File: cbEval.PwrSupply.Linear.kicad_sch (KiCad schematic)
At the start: 34 parts, among them J1 CAL.CT3151V1-0, J11 Bergstik-II_6, J12 Header.Hor.2x8.9-103326-0-08, J13 Header.Hor.2x8.9-103326-0-08, J2 CAL.CT3151V1-2, J3 Socket.Hor.2x8.1-5535512-8, J4 Socket.Hor.2x8.1-5535512-8, U1 MIC29151-5.0WU, U2 MIC29151-3.3WU, U3 DS1834AS+

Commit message: Properties geändert, Logo aktualisiert
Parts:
- removed MP1: KiCAD-Logo2.5mm.SilkScreen, Symbol:KiCad-Logo2_5mm_SilkScreen, symbol Symbol:KiCAD-Logo2.5mm.SilkScreen
- added MP1: KiCAD-DesignedWith-Logo2.5mm.SilkScreen, Symbol:KiCad-Logo2_5mm_SilkScreen, symbol Symbol:KiCAD-DesignedWith-Logo2.5mm.SilkScreen
- J12, J3: Usage Usage -> Pwr Bus
- J13, J4: Usage Usage -> Data Bus
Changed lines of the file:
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@@
-    )
-  )
-  (symbol (lib_id "Symbol:KiCAD-Logo2.5mm.SilkScreen") (at 55.88 15.24 0) (unit 1)
-    (in_bom yes) (on_board yes)
-    (property "Reference" "MP1" (id 0) (at 55.88 15.24 0))
-    (property "Value" "KiCAD-Logo2.5mm.SilkScreen" (id 1) (at 55.88 17.78 0))
-    (property "Footprint" "Symbol:KiCad-Logo2_5mm_SilkScreen" (id 2) (at 55.88 12.7 0)
-      (effects (font (size 1.27 1.27)) hide)
-    )
-    (property "Datasheet" "" (id 3) (at 55.88 15.24 0)
-      (effects (font (size 1.27 1.27)) hide)
     )
   )
@@
     )
     (pin "1")
+  )
+  (symbol (lib_id "Symbol:KiCAD-DesignedWith-Logo2.5mm.SilkScreen") (at 55.88 15.24 0) (unit 1)
+    (in_bom yes) (on_board yes)
+    (property "Reference" "MP1" (id 0) (at 55.88 15.24 0))
+    (property "Value" "KiCAD-DesignedWith-Logo2.5mm.SilkScreen" (id 1) (at 55.88 17.78 0))
+    (property "Footprint" "Symbol:KiCad-Logo2_5mm_SilkScreen" (id 2) (at 55.88 12.7 0)
+      (effects (font (size 1.27 1.27)) hide)
+    )
+    (property "Datasheet" "" (id 3) (at 55.88 15.24 0)
+      (effects (font (size 1.27 1.27)) hide)
+    )
   )
   (symbol (lib_id "Supply:GND") (at 33.02 193.04 0) (unit 1)
@@
     (pin "2")
   )
-  (symbol (lib_name "C.Nichicon.UWT.35V:100µ_1") (lib_id "C.Nichicon.UWT.35V:100µ") (at 104.14 48.26 0) (mirror y) (unit 1)
+  (symbol (lib_id "C.Nichicon.UWT.35V:100µ") (at 104.14 48.26 0) (mirror y) (unit 1)
     (in_bom yes) (on_board yes)
     (property "Reference" "C1" (id 0) (at 101.6 43.18 0)
@@
       (effects (font (size 1.016 1.016)) hide)
     )
-    (property "Usage" "Usage" (id 4) (at 76.2 193.04 0))
+    (property "Usage" "Pwr Bus" (id 4) (at 76.2 193.04 0))
     (property "ID" "1-5535512-8" (id 5) (at 80.01 171.45 90)
       (effects (font (size 0.635 0.635) italic))
@@
       (effects (font (size 1.016 1.016)) hide)
     )
-    (property "Usage" "Usage" (id 4) (at 152.4 193.04 0))
+    (property "Usage" "Data Bus" (id 4) (at 152.4 193.04 0))
     (property "ID" "1-5535512-8" (id 5) (at 156.21 171.45 90)
       (effects (font (size 0.635 0.635) italic))
@@
       (effects (font (size 1.016 1.016)) hide)
     )
-    (property "Usage" "Usage" (id 4) (at 25.4 193.04 0))
+    (property "Usage" "Pwr Bus" (id 4) (at 25.4 193.04 0))
     (property "ID" "9-103326-0-08" (id 5) (at 21.59 171.45 90)
       (effects (font (size 0.635 0.635) italic))
@@
       (effects (font (size 1.016 1.016)) hide)
     )
-    (property "Usage" "Usage" (id 4) (at 109.22 193.04 0))
+    (property "Usage" "Data Bus" (id 4) (at 109.22 193.04 0))
     (property "ID" "9-103326-0-08" (id 5) (at 105.41 171.45 90)
       (effects (font (size 0.635 0.635) italic))
@@
       (reference "J13") (unit 1) (value "Header.Hor.2x8.9-103326-0-08") (footprint "Connector_PinHeader_2.54mm:PinHeader_2x08_P2.54mm_Horizontal")
     )
-    (path "/aa3513d0-0eee-457c-a792-7c9954431f2c"
-      (reference "MP1") (unit 1) (value "KiCAD-Logo2.5mm.SilkScreen") (footprint "Symbol:KiCad-Logo2_5mm_SilkScreen")
+    (path "/c9e57e62-be33-4183-8d54-8f35a9c1b2d9"
+      (reference "MP1") (unit 1) (value "KiCAD-DesignedWith-Logo2.5mm.SilkScreen") (footprint "Symbol:KiCad-Logo2_5mm_SilkScreen")
     )
     (path "/92587325-892b-4776-9d98-5bf9e0f65dcf"

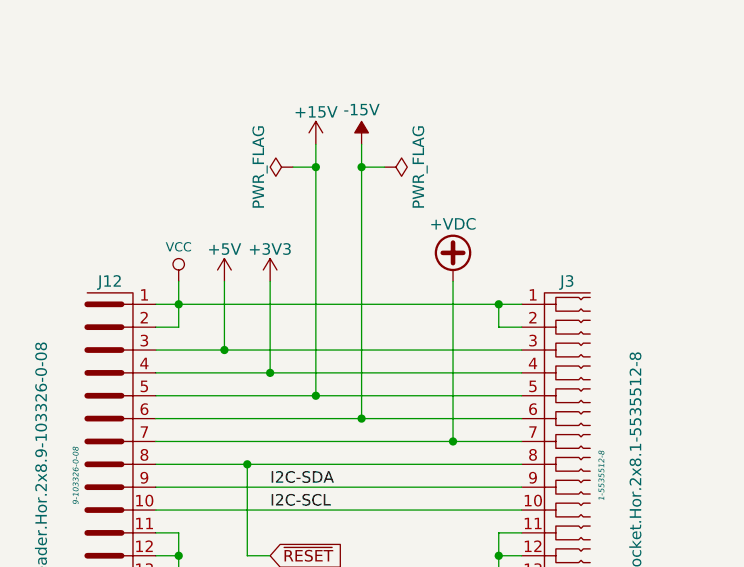
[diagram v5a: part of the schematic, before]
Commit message: Stromversorgung korrigiert (5P/3P3)
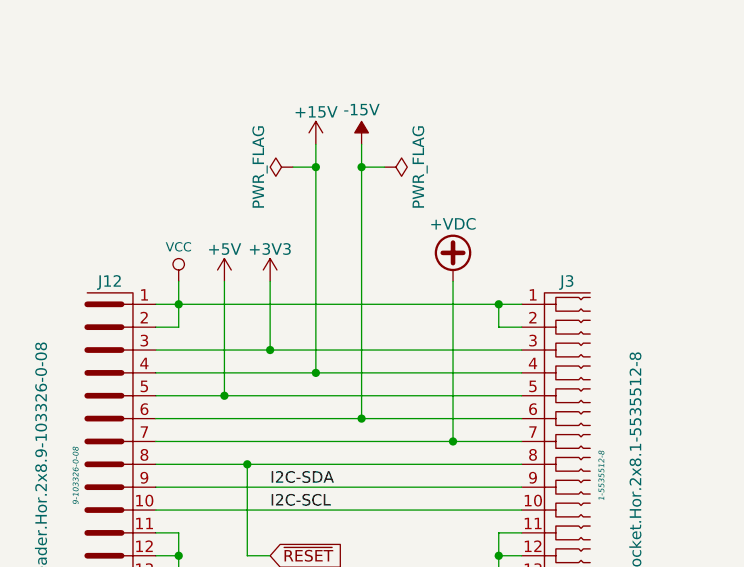
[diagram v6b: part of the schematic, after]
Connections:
- net +15V: now also J12.4, J3.4; no longer J12.5, J3.5
- net +3V3: now also J12.3, J3.3; no longer J12.4, J3.4
- net +5V: now also J12.5, J3.5; no longer J12.3, J3.3
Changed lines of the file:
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@@
-(kicad_sch (version 20210126) (generator eeschema)
+(kicad_sch (version 20210406) (generator eeschema)
   (paper "A4")
   (title_block
     (title "cbEval PSupply 5P/3P3")
-    (rev "1.0.0")
+    (rev "1.1.0")
   )
   (junction (at 33.02 152.4) (diameter 0.9144) (color 0 0 0 0))
@@
   (junction (at 35.56 73.66) (diameter 0.9144) (color 0 0 0 0))
   (junction (at 35.56 99.06) (diameter 0.9144) (color 0 0 0 0))
-  (junction (at 38.1 157.48) (diameter 0.9144) (color 0 0 0 0))
+  (junction (at 38.1 162.56) (diameter 0.9144) (color 0 0 0 0))
   (junction (at 40.64 170.18) (diameter 0.9144) (color 0 0 0 0))
-  (junction (at 43.18 160.02) (diameter 0.9144) (color 0 0 0 0))
+  (junction (at 43.18 157.48) (diameter 0.9144) (color 0 0 0 0))
   (junction (at 48.26 137.16) (diameter 0.9144) (color 0 0 0 0))
-  (junction (at 48.26 162.56) (diameter 0.9144) (color 0 0 0 0))
+  (junction (at 48.26 160.02) (diameter 0.9144) (color 0 0 0 0))
   (junction (at 53.34 137.16) (diameter 0.9144) (color 0 0 0 0))
   (junction (at 53.34 165.1) (diameter 0.9144) (color 0 0 0 0))
@@
     (stroke (width 0) (type solid) (color 0 0 0 0))
   )
-  (wire (pts (xy 30.48 157.48) (xy 38.1 157.48))
-    (stroke (width 0) (type solid) (color 0 0 0 0))
-  )
-  (wire (pts (xy 30.48 160.02) (xy 43.18 160.02))
-    (stroke (width 0) (type solid) (color 0 0 0 0))
-  )
-  (wire (pts (xy 30.48 162.56) (xy 48.26 162.56))
+  (wire (pts (xy 30.48 160.02) (xy 48.26 160.02))
+    (stroke (width 0) (type solid) (color 0 0 0 0))
+  )
+  (wire (pts (xy 30.48 162.56) (xy 38.1 162.56))
     (stroke (width 0) (type solid) (color 0 0 0 0))
   )
@@
     (stroke (width 0) (type solid) (color 0 0 0 0))
   )
-  (wire (pts (xy 38.1 149.86) (xy 38.1 157.48))
-    (stroke (width 0) (type solid) (color 0 0 0 0))
-  )
-  (wire (pts (xy 38.1 157.48) (xy 71.12 157.48))
+  (wire (pts (xy 38.1 149.86) (xy 38.1 162.56))
+    (stroke (width 0) (type solid) (color 0 0 0 0))
+  )
+  (wire (pts (xy 38.1 162.56) (xy 71.12 162.56))
     (stroke (width 0) (type solid) (color 0 0 0 0))
   )
@@
     (stroke (width 0) (type solid) (color 0 0 0 0))
   )
-  (wire (pts (xy 43.18 149.86) (xy 43.18 160.02))
-    (stroke (width 0) (type solid) (color 0 0 0 0))
-  )
-  (wire (pts (xy 43.18 160.02) (xy 71.12 160.02))
+  (wire (pts (xy 43.18 149.86) (xy 43.18 157.48))
+    (stroke (width 0) (type solid) (color 0 0 0 0))
+  )
+  (wire (pts (xy 43.18 157.48) (xy 30.48 157.48))
+    (stroke (width 0) (type solid) (color 0 0 0 0))
+  )
+  (wire (pts (xy 43.18 157.48) (xy 71.12 157.48))
     (stroke (width 0) (type solid) (color 0 0 0 0))
   )
@@
     (stroke (width 0) (type solid) (color 0 0 0 0))
   )
-  (wire (pts (xy 48.26 137.16) (xy 48.26 162.56))
-    (stroke (width 0) (type solid) (color 0 0 0 0))
-  )
-  (wire (pts (xy 48.26 162.56) (xy 71.12 162.56))
-    (stroke (width 0) (type solid) (color 0 0 0 0))
-  )
+  (wire (pts (xy 48.26 137.16) (xy 48.26 160.02))
+    (stroke (width 0) (type solid) (color 0 0 0 0))
+  )
+  (wire (pts (xy 48.26 160.02) (xy 71.12 160.02))
+    (stroke (width 0) (type solid) (color 0 0 0 0))
+  )

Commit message: gespeichert im neuen Format
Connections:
- net SPI-~CE renamed SPI-~{CE}
- net ~PWR-FAIL renamed ~{PWR-FAIL}
- net ~RESET renamed ~{RESET}
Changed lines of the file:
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@@
-(kicad_sch (version 20210406) (generator eeschema)
+(kicad_sch (version 20210621) (generator eeschema)
   (paper "A4")
   (title_block
@@
     (effects (font (size 1.27 1.27)) (justify left bottom))
   )
-  (label "SPI-~CE" (at 119.38 180.34 0)
+  (label "SPI-~{CE}" (at 119.38 180.34 0)
     (effects (font (size 1.27 1.27)) (justify left bottom))
   )
@@
     (effects (font (size 1.27 1.27)) (justify left bottom))
   )
-  (global_label "~RESET" (shape input) (at 43.18 180.34 0)
+  (global_label "~{RESET}" (shape input) (at 43.18 180.34 0)
     (effects (font (size 1.27 1.27)) (justify left))
     (property "Intersheet References" "${INTERSHEET_REFS}" (id 0) (at 51.3383 180.2606 0)
@@
     )
   )
-  (global_label "~PWR-FAIL" (shape input) (at 142.24 45.72 0)
+  (global_label "~{PWR-FAIL}" (shape input) (at 142.24 45.72 0)
     (effects (font (size 1.27 1.27)) (justify left))
     (property "Intersheet References" "${INTERSHEET_REFS}" (id 0) (at 154.0269 45.6406 0)
@@
     )
   )
-  (global_label "~PWR-FAIL" (shape input) (at 142.24 91.44 0)
+  (global_label "~{PWR-FAIL}" (shape input) (at 142.24 91.44 0)
     (effects (font (size 1.27 1.27)) (justify left))
     (property "Intersheet References" "${INTERSHEET_REFS}" (id 0) (at 154.0269 91.3606 0)
@@
     )
   )
-  (global_label "~PWR-FAIL" (shape input) (at 231.14 139.7 180)
+  (global_label "~{PWR-FAIL}" (shape input) (at 231.14 139.7 180)
     (effects (font (size 1.27 1.27)) (justify right))
     (property "Intersheet References" "${INTERSHEET_REFS}" (id 0) (at 219.3531 139.6206 0)
@@
     )
   )
-  (global_label "~RESET" (shape input) (at 271.78 132.08 0)
+  (global_label "~{RESET}" (shape input) (at 271.78 132.08 0)
     (effects (font (size 1.27 1.27)) (justify left))
     (property "Intersheet References" "${INTERSHEET_REFS}" (id 0) (at 279.9383 132.0006 0)
